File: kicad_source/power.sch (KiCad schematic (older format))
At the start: 16 parts, among them SW5 SWITCH_INV, U5 TPS736XX, U6 TPS736XX

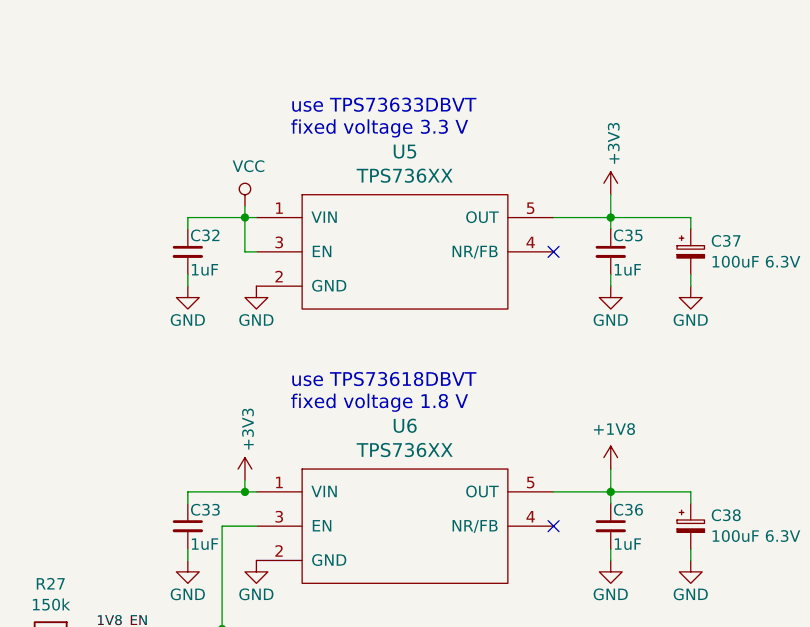
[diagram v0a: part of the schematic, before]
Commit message: added some missing part numbers
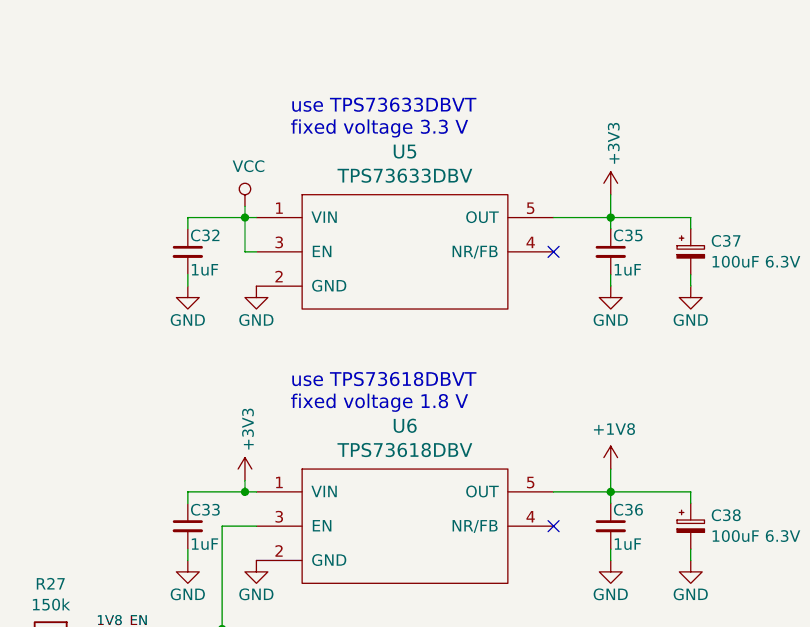
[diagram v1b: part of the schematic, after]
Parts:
- U5: value TPS736XX -> TPS73633DBV
- U6: value TPS736XX -> TPS73618DBV
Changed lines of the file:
@@
 AR Path="/5EB35F1D/5CB4F8EB" Ref="U5"  Part="1"
 F 0 "U5" H 4300 4437 60  0000 C CNN
-F 1 "TPS736XX" H 4300 4331 60  0000 C CNN
+F 1 "TPS73633DBV" H 4300 4331 60  0000 C CNN
 F 2 "SOT_TO:SOT-23-5" H 4300 4200 60  0001 C CNN
 F 3 "" H 4300 4050 60  0000 C CNN
@@
 AR Path="/5EB35F1D/5EB83C7C" Ref="U6"  Part="1"
 F 0 "U6" H 4300 5637 60  0000 C CNN
-F 1 "TPS736XX" H 4300 5531 60  0000 C CNN
+F 1 "TPS73618DBV" H 4300 5531 60  0000 C CNN
 F 2 "SOT_TO:SOT-23-5" H 4300 5400 60  0001 C CNN
 F 3 "" H 4300 5250 60  0000 C CNN

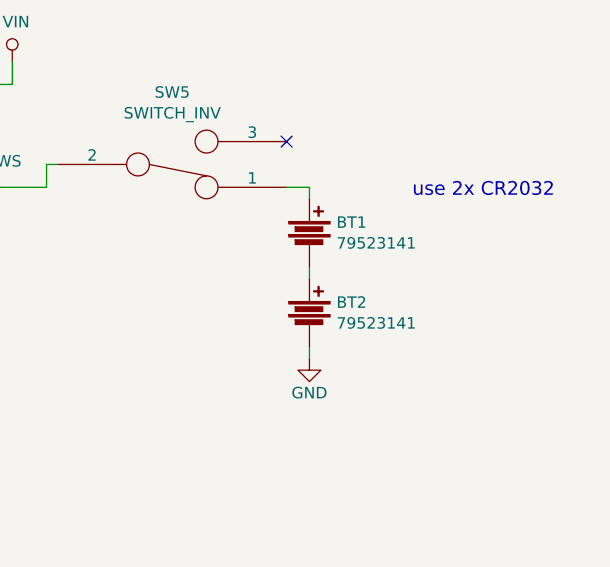
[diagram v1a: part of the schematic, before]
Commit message: changed BMA400 to BMA253, changed SD-Card-Socket to MEM2061-01-188-00-A and changed battery holder to BAT-HLD-001 for cost reduction
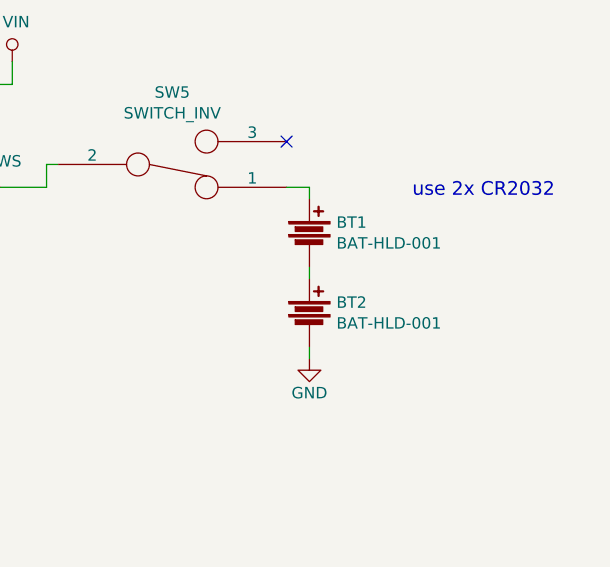
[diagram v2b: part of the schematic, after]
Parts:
- BT1, BT2: value 79523141 -> BAT-HLD-001
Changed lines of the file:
@@
 AR Path="/5EB35F1D/5CB4F961" Ref="BT1"  Part="1"
 F 0 "BT1" H 7068 2046 50  0000 L CNN
-F 1 "79523141" H 7068 1955 50  0000 L CNN
+F 1 "BAT-HLD-001" H 7068 1955 50  0000 L CNN
 F 2 "MECH_battery_holder:Wuerth_WA-BCMC_79523141" V 6950 2040 50  0001 C CNN
 F 3 "" V 6950 2040 50  0000 C CNN
@@
 AR Path="/5EB35F1D/5ECE9E11" Ref="BT2"  Part="1"
 F 0 "BT2" H 7068 2396 50  0000 L CNN
-F 1 "79523141" H 7068 2305 50  0000 L CNN
+F 1 "BAT-HLD-001" H 7068 2305 50  0000 L CNN
 F 2 "MECH_battery_holder:Wuerth_WA-BCMC_79523141" V 6950 2390 50  0001 C CNN
 F 3 "" V 6950 2390 50  0000 C CNN

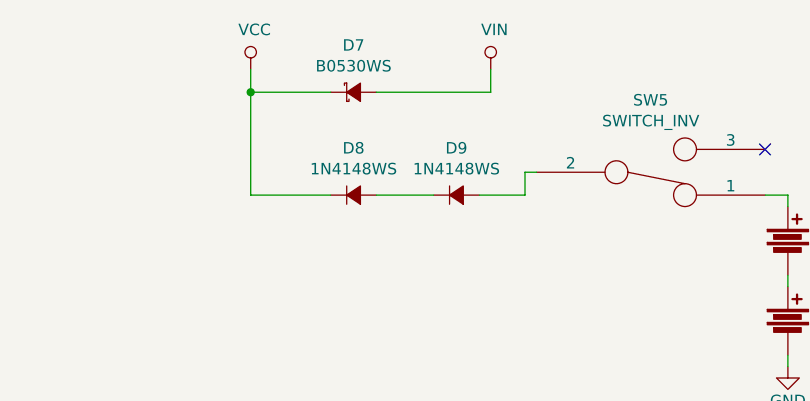
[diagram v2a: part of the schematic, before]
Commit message: optimized parts for BOM costs
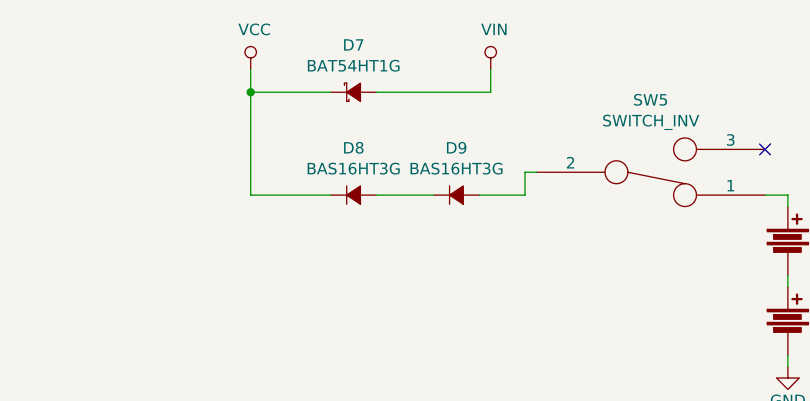
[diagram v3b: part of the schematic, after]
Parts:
- D7: value B0530WS -> BAT54HT1G
- D8, D9: value 1N4148WS -> BAS16HT3G
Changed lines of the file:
@@
 P 5500 1800
 F 0 "D9" H 5500 2005 50  0000 C CNN
-F 1 "1N4148WS" H 5500 1914 50  0000 C CNN
+F 1 "BAS16HT3G" H 5500 1914 50  0000 C CNN
 F 2 "diodes:SOD-323" V 5500 1800 50  0001 C CNN
 F 3 "" V 5500 1800 50  0000 C CNN
@@
 P 5050 1800
 F 0 "D8" H 5050 2005 50  0000 C CNN
-F 1 "1N4148WS" H 5050 1914 50  0000 C CNN
+F 1 "BAS16HT3G" H 5050 1914 50  0000 C CNN
 F 2 "diodes:SOD-323" V 5050 1800 50  0001 C CNN
 F 3 "" V 5050 1800 50  0000 C CNN
@@
 P 5050 1350
 F 0 "D7" H 5050 1555 50  0000 C CNN
-F 1 "B0530WS" H 5050 1464 50  0000 C CNN
+F 1 "BAT54HT1G" H 5050 1464 50  0000 C CNN
 F 2 "diodes:SOD-323" V 5050 1350 50  0001 C CNN
 F 3 "" V 5050 1350 50  0000 C CNN
